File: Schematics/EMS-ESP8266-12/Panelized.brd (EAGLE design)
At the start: 97.8 x 76.2 mm, 86 parts, among them IC1 LM393N, IC2 LM393N, T1 BC547B, T2 BC547B, T3 BC547B, T4 BC547B

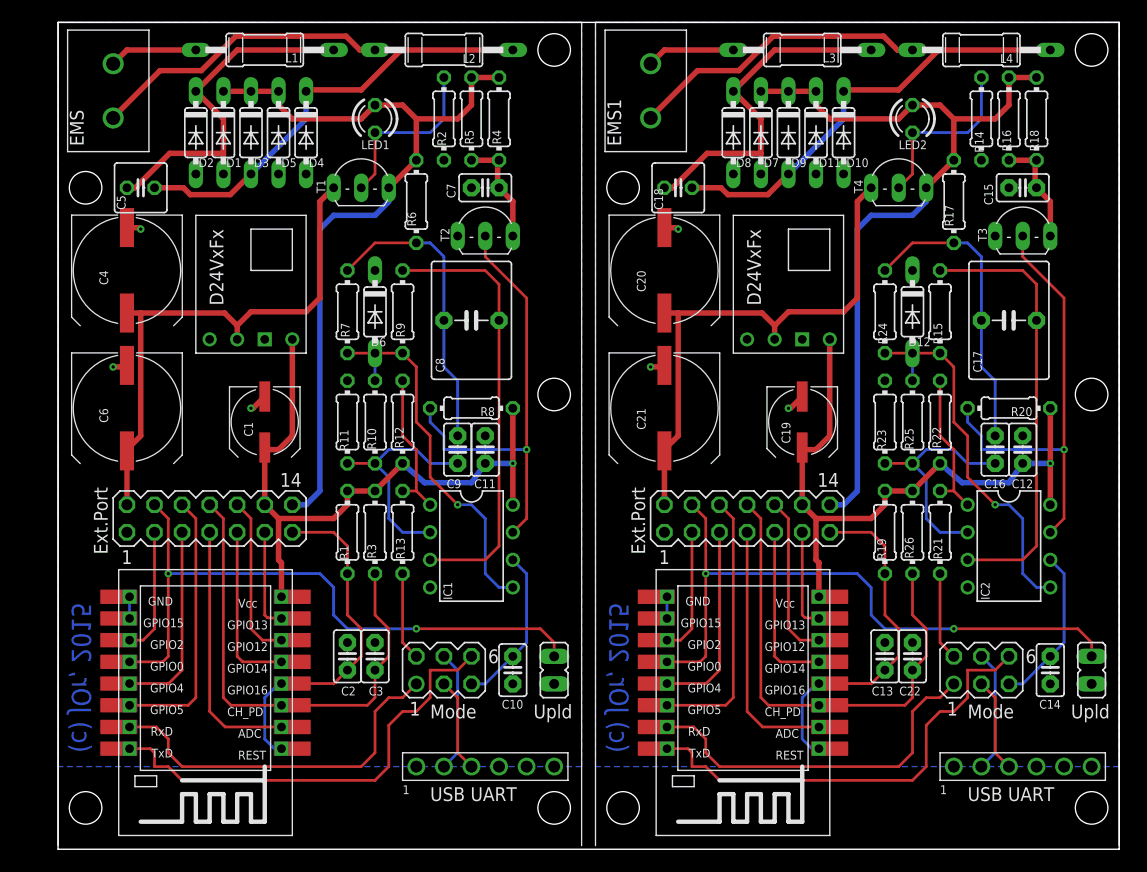
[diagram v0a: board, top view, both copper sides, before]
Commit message: - add panelized Board for Rev 1.0b
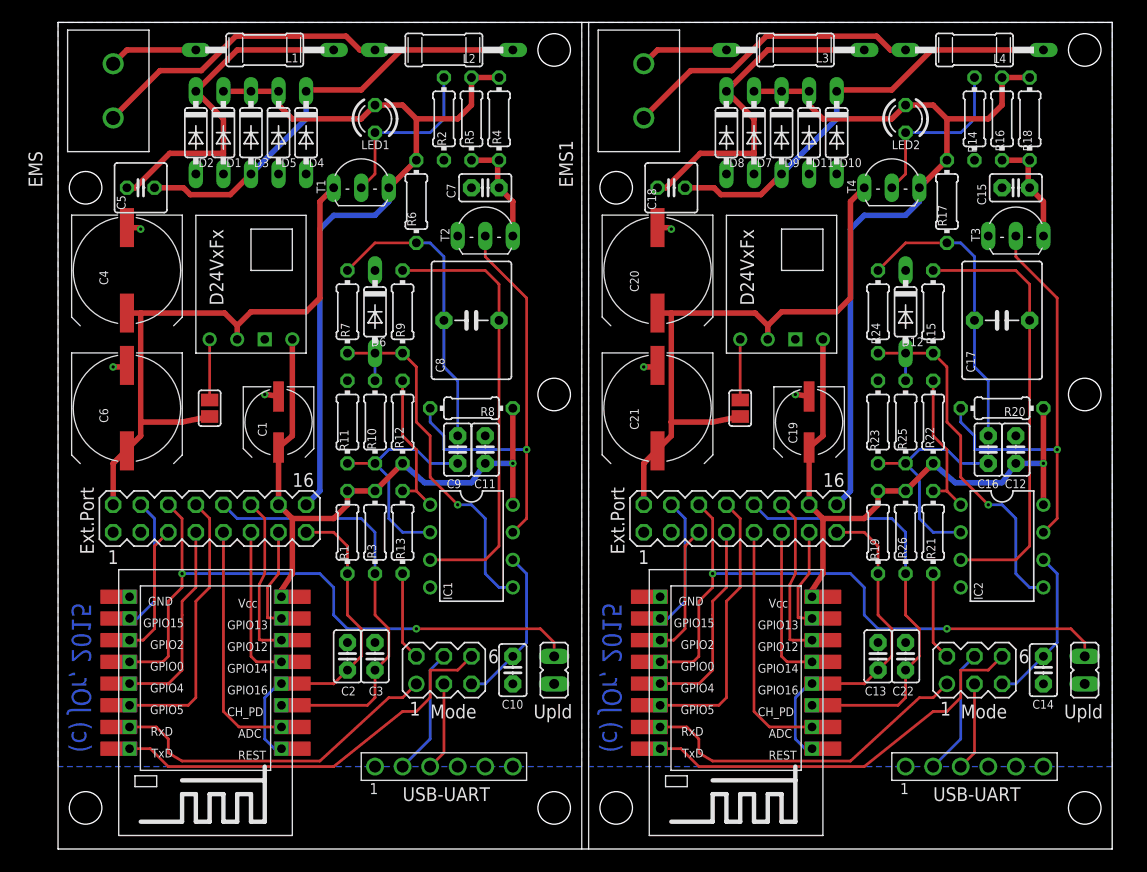
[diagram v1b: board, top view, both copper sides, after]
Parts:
- removed MODE1: (no value), con-lstb:MA03-2
- added SJ1, SJ2: n.u., jumper:SJ
- added SV2: Mode, con-lstb:MA03-2
- EMS, EMS1: value EMS -> 691102710002
- EXT.PORT, EXT.PORT1: device con-lstb:MA07-2 -> con-lstb:MA08-2
- SV1: value (none) -> Mode
- moved PROGRAM1 4.45 mm to (84.5, 7.62)
- moved PROGRAM 3.81 mm to (35.6, 7.62)
- moved C1 1.27 mm to (20.3, 39.4)
- moved C12 0.64 mm to (88.3, 36.8)
- moved C13 0.64 mm to (75.6, 17.8)
- moved C15 0.64 mm to (88.3, 61.0)
- moved C16 0.64 mm to (85.7, 36.8)
- moved C19 0.64 mm to (69.2, 39.4)
- moved C20 0.64 mm to (55.2, 53.3)
- moved C21 0.64 mm to (55.2, 40.6)
- moved D10 0.64 mm to (71.8, 66.0)
- moved D9 0.64 mm to (66.7, 66.0)
- moved ESP2 0.64 mm to (70.5, 1.27)
- moved L3 0.64 mm to (67.9, 73.7)
- moved L4 0.64 mm to (84.5, 73.7)
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- renumbered MODE to SV1
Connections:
- new net N$24: MOD2./SHDN, SJ2.1
- new net N$3: MOD1./SHDN, SJ1.1
- net +3V1: now also EXT.PORT1.14; no longer EXT.PORT1.12
- net +3V3: now also EXT.PORT.14; no longer EXT.PORT.12
- net ADC: now also EXT.PORT.9; no longer EXT.PORT.7
- net ADC1: now also EXT.PORT1.9; no longer EXT.PORT1.7
- net CH_PD: now also EXT.PORT.10; no longer EXT.PORT.8
- net CH_PD1: now also EXT.PORT1.10; no longer EXT.PORT1.8
- net EMS_RX1: now also SV2.5; no longer MODE1.5
- net EMS_TX1: now also SV2.2; no longer MODE1.2
- net GND: now also ESP1.GND, EXT.PORT.3
- net GND1: now also ESP2.GND, EXT.PORT1.3
- net GPIO0: now also EXT.PORT.6; no longer EXT.PORT.4
- net GPIO1: now also EXT.PORT1.5; no longer EXT.PORT1.3
- net GPIO10: now also ESP2.GPIO5, EXT.PORT1.8; no longer ESP2.GND, ESP2.GPIO15
- net GPIO11: now also ESP2.GPIO15, EXT.PORT1.4; no longer ESP2.GPIO5, EXT.PORT1.6
- net GPIO12: now also EXT.PORT.12; no longer EXT.PORT.10
- net GPIO13: now also EXT.PORT.13; no longer EXT.PORT.11
- net GPIO14: now also EXT.PORT.11; no longer EXT.PORT.9
- net GPIO15: now also EXT.PORT.4; no longer ESP1.GND
- net GPIO2: now also EXT.PORT.5; no longer EXT.PORT.3
- net GPIO3: now also EXT.PORT1.7; no longer EXT.PORT1.5
- net GPIO4: now also EXT.PORT.7; no longer EXT.PORT.5
- net GPIO5: now also EXT.PORT.8; no longer EXT.PORT.6
- net GPIO6: now also EXT.PORT1.13; no longer EXT.PORT1.11
- net GPIO7: now also EXT.PORT1.12; no longer EXT.PORT1.10
- net GPIO8: now also EXT.PORT1.11; no longer EXT.PORT1.9
- net GPIO9: now also EXT.PORT1.6; no longer EXT.PORT1.4
- net REST: now also EXT.PORT.15; no longer EXT.PORT.13
- net REST1: now also EXT.PORT1.15; no longer EXT.PORT1.13
- net RXD1: now also SV2.4; no longer MODE1.4
- net TXD1: now also SV2.3; no longer MODE1.3
- net UBUCK: now also SJ1.2
- net UBUCK1: now also SJ2.2
- net UEMS: now also EXT.PORT.16; no longer EXT.PORT.14
- net UEMS1: now also EXT.PORT1.16; no longer EXT.PORT1.14
- net URXD1: now also SV2.1; no longer MODE1.1
- net UTXD1: now also SV2.6; no longer MODE1.6
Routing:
- net GPIO10: track 2.00 -> 25.2 mm
- net GPIO11: track 24.7 -> 12.4 mm
- net GPIO15: track 2.00 -> 12.4 mm
- net UBUCK1: track 49.5 -> 56.5 mm
- net UBUCK: track 49.5 -> 56.5 mm
- net N$3: track 0.00 -> 5.59 mm
- net N$24: track 0.00 -> 5.59 mm
- net CH_PD1: track 45.3 -> 40.2 mm
- net CH_PD: track 45.3 -> 40.2 mm
- net UTXD: track 41.9 -> 37.6 mm
- net UTXD1: track 41.9 -> 37.6 mm
- net URXD: track 34.1 -> 31.2 mm
- net URXD1: track 34.1 -> 31.2 mm
- net +3V1: track 61.3 -> 58.8 mm
- net +3V3: track 61.3 -> 58.8 mm
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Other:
- board size 97.8 x 76.2 mm -> 97.1 x 76.2 mm
- board text added: "EMS-ESP8266/12 Rev 1.0b"
- board text added: "USB-UART"
- board text removed: "EMS-ESP8266/12 Rev 1.0"
- board text removed: "USB UART"

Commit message: initial checkin for ems related files
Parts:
- renumbered C12 to C11', C13 to C2', C14 to C10', C15 to C7', C16 to C9', C17 to C8', C18 to C5', C19 to C1', C20 to C4', C21 to C6', C22 to C3', D10 to D4', D11 to D5', D12 to D6', D7 to D1', D8 to D2', D9 to D3', IC2 to IC1', L3 to L1', L4 to L2', LED2 to LED1', R14 to R2', R15 to R9', R16 to R5', R17 to R6', R18 to R4', R19 to R1', R20 to R8', R21 to R13', R22 to R12', R23 to R11', R24 to R7', R25 to R10', R26 to R3', T3 to T2', T4 to T1'
